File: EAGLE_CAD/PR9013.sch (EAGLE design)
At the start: 70 parts, among them J1 M3_SCREW_POST

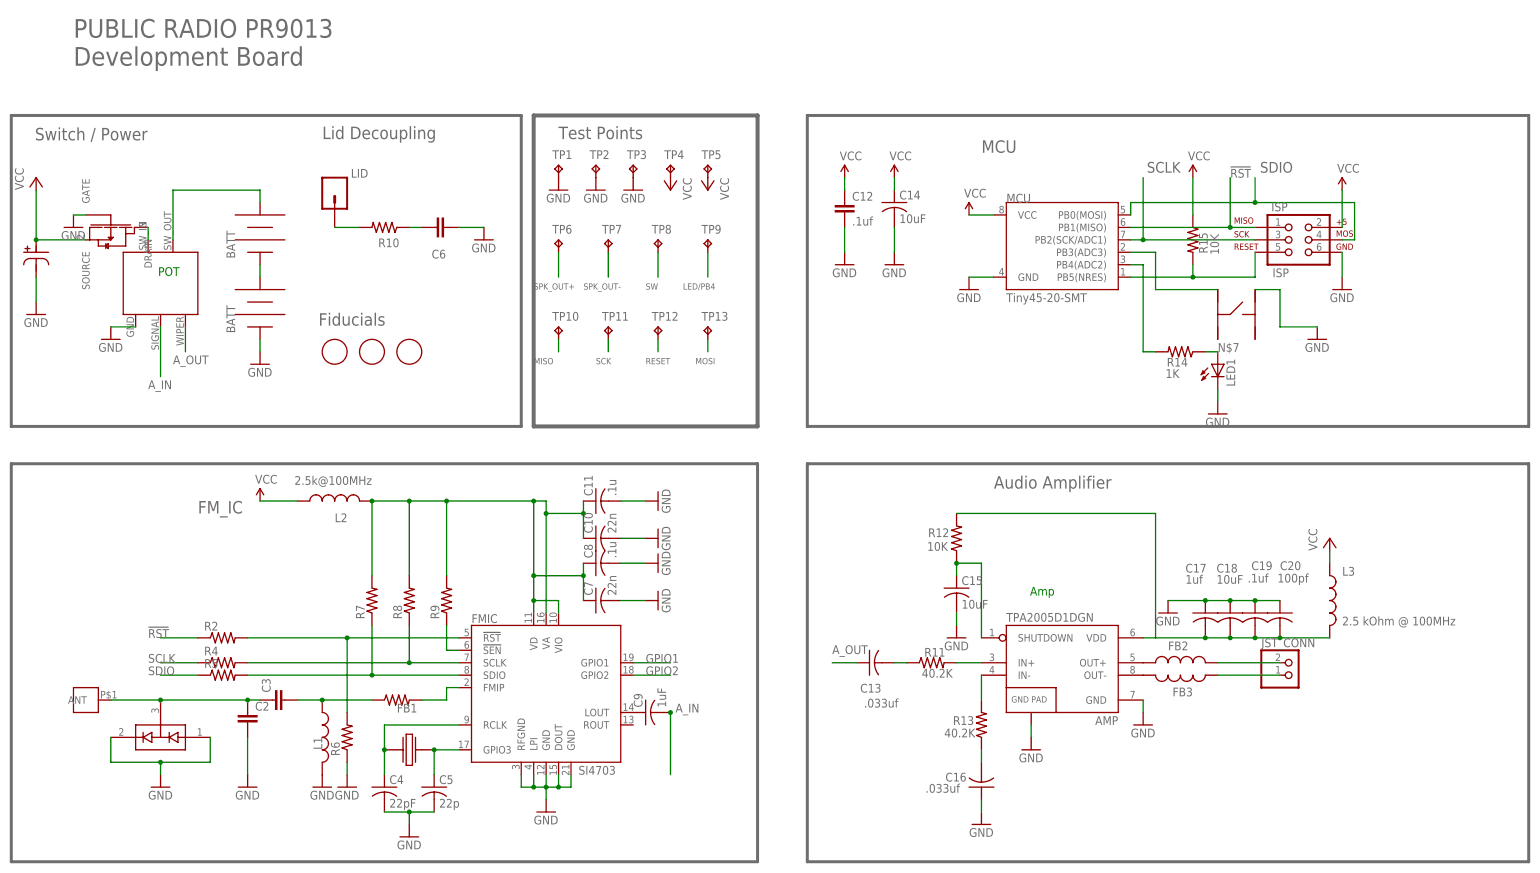
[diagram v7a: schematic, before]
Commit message: more routing changes
cleaned up amp section a bunch. feeling good about it.

also changed a bunch of packages down to 0402

and

re-routed the AVR area a bunch.
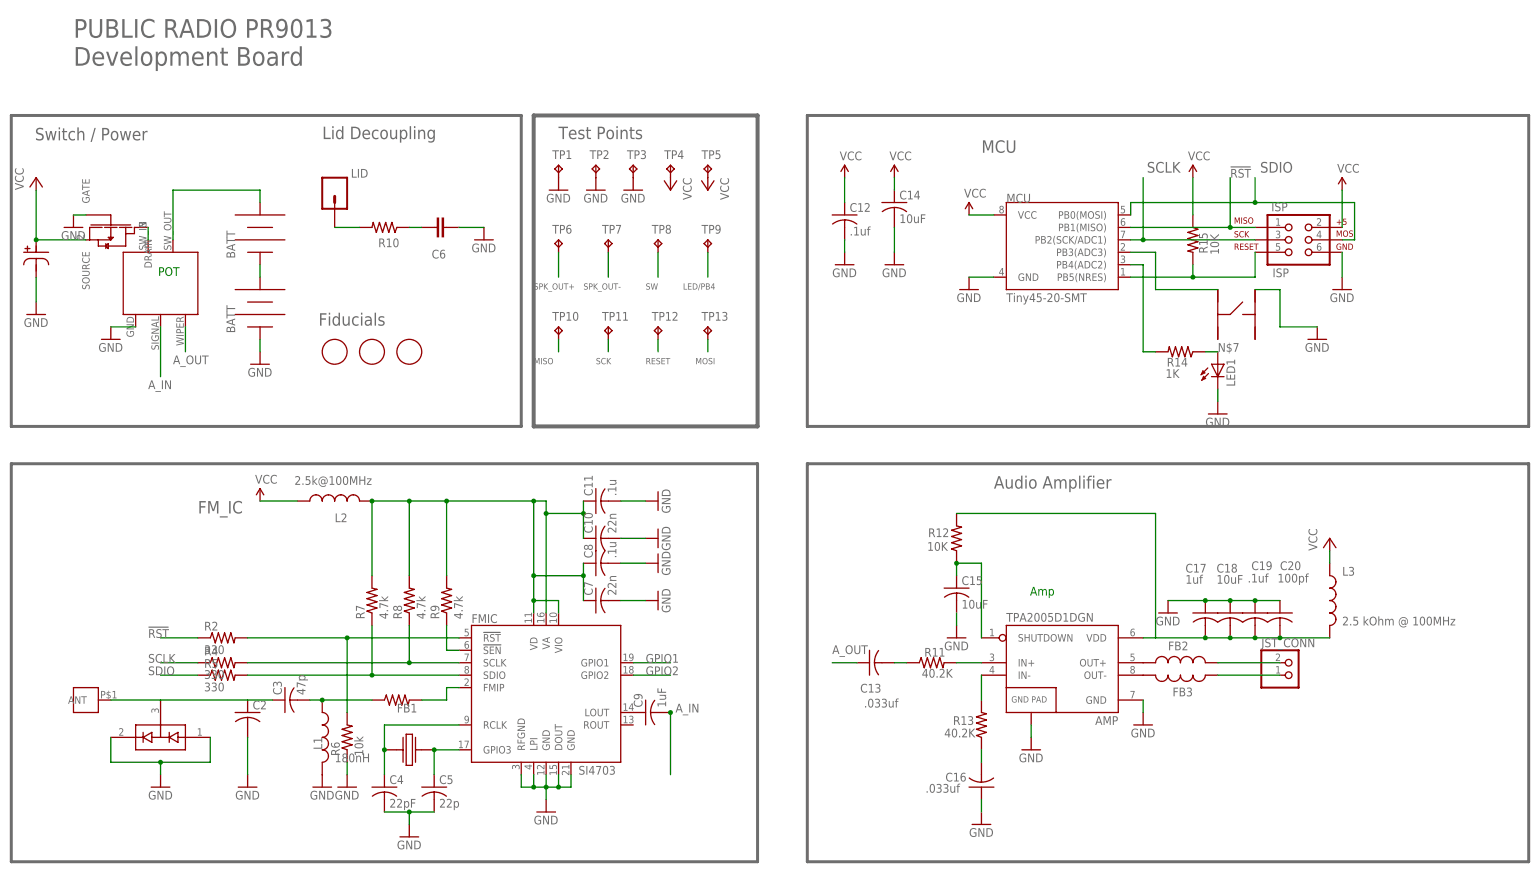
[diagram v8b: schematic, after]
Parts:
- C1: value NICHICON_SERIESUD -> 220uF
- C12: device SparkFun-Passives:CAP0805 -> resistor:C-USC0402
- C17, C9: device resistor:C-USC0402K -> resistor:C-USC0402
- C2: device SparkFun-Passives:CAP0603-CAP -> resistor:C-USC0402
- C3: value (none) -> 47p; device SparkFun-Passives:CAP0603-CAP -> resistor:C-USC0402
- FB2, FB3: device SparkFun-Passives:INDUCTOR0805 -> SparkFun-Passives:INDUCTOR0603
- L1: value (none) -> 180nH; device SparkFun-Passives:INDUCTOR0805 -> SparkFun-Passives:INDUCTOR0603
- R10: device SparkFun-Passives:RESISTOR0805-RES -> resistor:R-US_R0402
- R2, R4, R5: value (none) -> 330
- R6: value (none) -> 10k
- R7, R8, R9: value (none) -> 4.7k
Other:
- moved on the sheet: C12, C3
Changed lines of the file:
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@@
 <part name="R14" library="resistor" deviceset="R-US_" device="R0402" value="1K"/>
 <part name="GND6" library="SparkFun-Aesthetics" deviceset="GND" device=""/>
-<part name="L1" library="SparkFun-Passives" deviceset="INDUCTOR" device="0805"/>
+<part name="L1" library="SparkFun-Passives" deviceset="INDUCTOR" device="0603" value="180nH"/>
 <part name="GND21" library="SparkFun" deviceset="GND" device=""/>
 <part name="GND16" library="SparkFun" deviceset="GND" device=""/>
-<part name="C12" library="SparkFun-Passives" deviceset="CAP" device="0805" value=".1uf"/>
+<part name="C12" library="resistor" deviceset="C-US" device="C0402" value=".1uf"/>
 <part name="C19" library="resistor" deviceset="C-US" device="C0402" value=".1uf"/>
 <part name="C20" library="resistor" deviceset="C-US" device="C0402" value="100pf"/>
 <part name="LID" library="SparkFun-Connectors" deviceset="M01" device="PTH"/>
 <part name="C6" library="SparkFun-Passives" deviceset="CAP" device="0805"/>
-<part name="R10" library="SparkFun-Passives" deviceset="RESISTOR" device="0805-RES"/>
+<part name="R10" library="resistor" deviceset="R-US_" device="R0402"/>
 <part name="D1" library="SparkFun-DiscreteSemi" deviceset="BAV99" device=""/>
 <part name="JP5" library="PR_Parts_Library" deviceset="BK-92_MPD_AA_BATT_CLIP" device=""/>
@@
 <part name="GND10" library="SparkFun-Aesthetics" deviceset="GND" device=""/>
 <part name="FB1" library="resistor" deviceset="R-US_" device="R0402"/>
-<part name="FB2" library="SparkFun-Passives" deviceset="INDUCTOR" device="0805"/>
-<part name="FB3" library="SparkFun-Passives" deviceset="INDUCTOR" device="0805"/>
+<part name="FB2" library="SparkFun-Passives" deviceset="INDUCTOR" device="0603"/>
+<part name="FB3" library="SparkFun-Passives" deviceset="INDUCTOR" device="0603"/>
 <part name="R15" library="resistor" deviceset="R-US_" device="R0402" value="10K"/>
 <part name="SUPPLY1" library="SparkFun-Aesthetics" deviceset="VCC" device=""/>
 <part name="JST_CONN" library="adafruit" deviceset="JST_2PIN" device="-SMT-RA"/>
-<part name="C2" library="SparkFun-Passives" deviceset="CAP" device="0603-CAP"/>
-<part name="C3" library="SparkFun-Passives" deviceset="CAP" device="0603-CAP"/>
+<part name="C2" library="resistor" deviceset="C-US" device="C0402"/>
+<part name="C3" library="resistor" deviceset="C-US" device="C0402" value="47p"/>
 <part name="C4" library="resistor" deviceset="C-US" device="C0402" value="22pF"/>
 <part name="C5" library="resistor" deviceset="C-US" device="C0402" value="22p"/>
 <part name="C7" library="resistor" deviceset="C-US" device="C0402" value="22n"/>
 <part name="C8" library="resistor" deviceset="C-US" device="C0402" value=".1u"/>
-<part name="R2" library="resistor" deviceset="R-US_" device="R0402"/>
-<part name="R4" library="resistor" deviceset="R-US_" device="R0402"/>
-<part name="R5" library="resistor" deviceset="R-US_" device="R0402"/>
-<part name="R8" library="resistor" deviceset="R-US_" device="R0402"/>
-<part name="R9" library="resistor" deviceset="R-US_" device="R0402"/>
-<part name="R7" library="resistor" deviceset="R-US_" device="R0402"/>
-<part name="R6" library="resistor" deviceset="R-US_" device="R0402"/>
+<part name="R2" library="resistor" deviceset="R-US_" device="R0402" value="330"/>
+<part name="R4" library="resistor" deviceset="R-US_" device="R0402" value="330"/>
+<part name="R5" library="resistor" deviceset="R-US_" device="R0402" value="330"/>
+<part name="R8" library="resistor" deviceset="R-US_" device="R0402" value="4.7k"/>
+<part name="R9" library="resistor" deviceset="R-US_" device="R0402" value="4.7k"/>
+<part name="R7" library="resistor" deviceset="R-US_" device="R0402" value="4.7k"/>
+<part name="R6" library="resistor" deviceset="R-US_" device="R0402" value="10k"/>
 <part name="C10" library="resistor" deviceset="C-US" device="C0402" value="22n"/>
 <part name="C11" library="resistor" deviceset="C-US" device="C0402" value=".1u"/>
 <part name="U$1" library="PR_Parts_Library" deviceset="C&amp;KPTS6465" device=""/>
-<part name="C1" library="PR_Parts_Library" deviceset="NICHICON_SERIESUD" device=""/>
+<part name="C1" library="PR_Parts_Library" deviceset="NICHICON_SERIESUD" device="" value="220uF"/>
 <part name="TP1" library="testpad" deviceset="TP" device="TP14R"/>
 <part name="TP2" library="testpad" deviceset="TP" device="TP14R"/>
@@
 <part name="C14" library="resistor" deviceset="C-US" device="C0603" value="10uF"/>
 <part name="C15" library="resistor" deviceset="C-US" device="C0603" value="10uF"/>
-<part name="C17" library="resistor" deviceset="C-US" device="C0402K" value="1uf"/>
-<part name="C9" library="resistor" deviceset="C-US" device="C0402K" value="1uF"/>
+<part name="C17" library="resistor" deviceset="C-US" device="C0402" value="1uf"/>
+<part name="C9" library="resistor" deviceset="C-US" device="C0402" value="1uF"/>
 </parts>
 <sheets>
@@
 <instance part="SUPPLY1" gate="1" x="200.66" y="139.7"/>
 <instance part="JST_CONN" gate="G$1" x="220.98" y="38.1"/>
-<instance part="C2" gate="G$1" x="7.62" y="27.94"/>
+<instance part="C2" gate="G$1" x="7.62" y="30.48"/>
 <instance part="C3" gate="G$1" x="15.24" y="33.02" rot="R90"/>
 <instance part="C4" gate="G$1" x="35.56" y="15.24"/>
@@
 <pinref part="GND22" gate="1" pin="GND"/>
 <pinref part="C12" gate="G$1" pin="2"/>
-<wire x1="129.54" y1="124.46" x2="129.54" y2="129.54" width="0.1524" layer="91"/>
+<wire x1="129.54" y1="124.46" x2="129.54" y2="127" width="0.1524" layer="91"/>
 </segment>
 <segment>
@@
 <pinref part="SUPPLY6" gate="1" pin="VCC"/>
 <pinref part="C12" gate="G$1" pin="1"/>
-<wire x1="129.54" y1="139.7" x2="129.54" y2="137.16" width="0.1524" layer="91"/>
+<wire x1="129.54" y1="139.7" x2="129.54" y2="134.62" width="0.1524" layer="91"/>
 </segment>
 <segment>
@@
 <pinref part="D1" gate="G$1" pin="COM"/>
 <wire x1="-20.32" y1="33.02" x2="-10.16" y2="33.02" width="0.1524" layer="91"/>
+<pinref part="C3" gate="G$1" pin="1"/>
+<pinref part="C2" gate="G$1" pin="1"/>
+<wire x1="7.62" y1="33.02" x2="12.7" y2="33.02" width="0.1524" layer="91"/>
 <wire x1="-10.16" y1="33.02" x2="7.62" y2="33.02" width="0.1524" layer="91"/>
-<junction x="-10.16" y="33.02"/>
-<pinref part="C2" gate="G$1" pin="1"/>
-<wire x1="7.62" y1="33.02" x2="10.16" y2="33.02" width="0.1524" layer="91"/>
-<junction x="7.62" y="33.02"/>
-<pinref part="C3" gate="G$1" pin="1"/>
 </segment>
 </net>
@@
 <segment>
 <pinref part="L1" gate="G$1" pin="1"/>
-<wire x1="17.78" y1="33.02" x2="22.86" y2="33.02" width="0.1524" layer="91"/>
+<wire x1="20.32" y1="33.02" x2="22.86" y2="33.02" width="0.1524" layer="91"/>
 <pinref part="FB1" gate="G$1" pin="1"/>
 <wire x1="33.02" y1="33.02" x2="22.86" y2="33.02" width="0.1524" layer="91"/>
